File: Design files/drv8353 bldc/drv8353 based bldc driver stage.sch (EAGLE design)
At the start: 80 parts, among them IC1 DRV8350RSRGZT, J3 2X6 FEMALE, J4 B06B-HCMKK

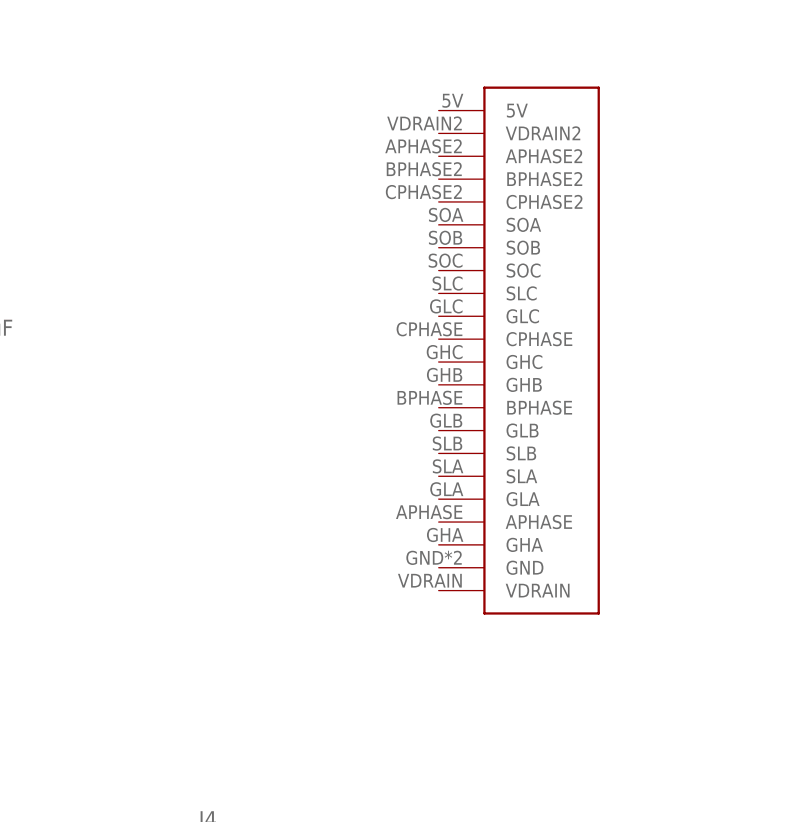
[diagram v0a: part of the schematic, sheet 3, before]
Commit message: reworked driver stage to work with board interface
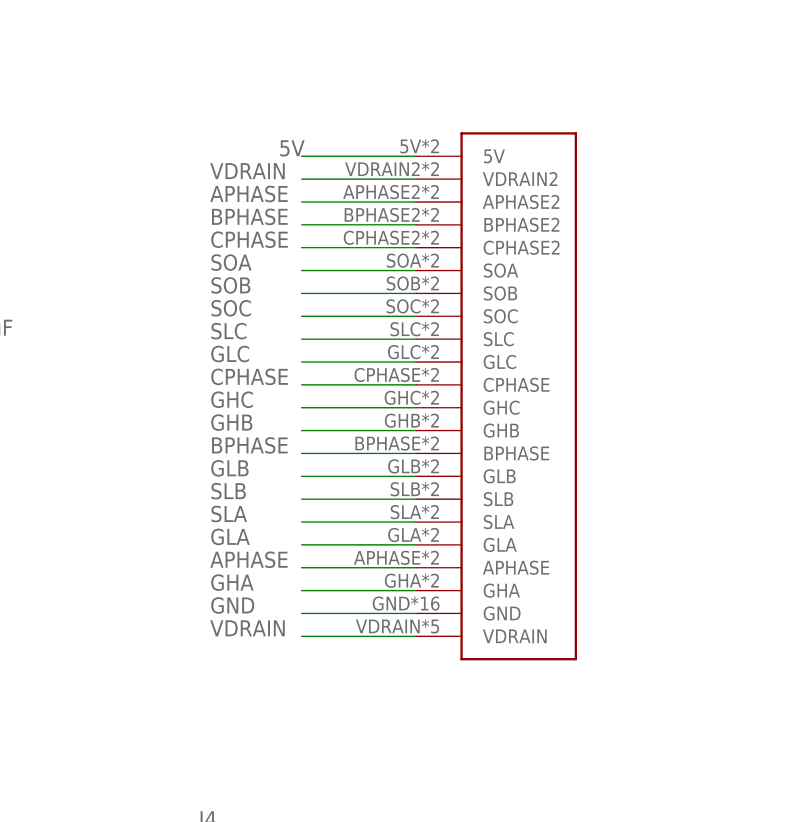
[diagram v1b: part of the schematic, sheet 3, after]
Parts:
- removed TP10, TP11, TP12, TP17, TP21, TP22, TP32, TP33, TP34, TP36, TP5, TP6, TP7, TP8, TP9: TPB1,27, testpad:TPB1,27
- U$3: value POWER_STAGE_CONNECTOR -> DRIVER_STAGE_CONNECTORDRIVER; device REV BLDC:POWER_STAGE_CONNECTOR -> REV BLDC:DRIVER_STAGE_CONNECTORDRIVER
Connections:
- net 5V: now also U$3.5V
- net APHASE: now also U$3.APHASE, U$3.APHASE2; no longer TP17.TP, TP32.TP
- net BPHASE: now also U$3.BPHASE, U$3.BPHASE2; no longer TP21.TP, TP6.TP
- net CPHASE: now also U$3.CPHASE, U$3.CPHASE2; no longer TP12.TP, TP22.TP
- net GHA: now also U$3.GHA; no longer TP36.TP
- net GHB: now also U$3.GHB; no longer TP8.TP
- net GHC: now also U$3.GHC; no longer TP9.TP
- net GLA: now also U$3.GLA; no longer TP33.TP
- net GLB: now also U$3.GLB; no longer TP7.TP
- net GLC: now also U$3.GLC; no longer TP11.TP
- net GND: now also U$3.GND
- net SLA: now also U$3.SLA; no longer TP34.TP
- net SLB: now also U$3.SLB; no longer TP5.TP
- net SLC: now also U$3.SLC; no longer TP10.TP
- net SOA: now also U$3.SOA
- net SOB: now also U$3.SOB
- net SOC: now also U$3.SOC
- net VDRAIN: now also U$3.VDRAIN, U$3.VDRAIN2
